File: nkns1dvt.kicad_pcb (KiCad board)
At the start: 2 copper layers, 180.4 x 132.8 mm, 76 parts, among them J1 MJ-4PP-9, J2 SERIAL_LED, SW1 SW_RESET, SW10 SW_PUSH, SW11 SW_PUSH, SW12 SW_PUSH, SW13 SW_PUSH, SW14 SW_PUSH, SW15 SW_PUSH, SW16 SW_PUSH, SW17 SW_PUSH, SW18 SW_PUSH, SW19 SW_PUSH, SW2 SW_PUSH, SW20 SW_PUSH, SW21 SW_PUSH, SW22 SW_PUSH, SW23 SW_PUSH, SW24 SW_PUSH, SW25 SW_PUSH, SW26 SW_PUSH, SW27 SW_PUSH, SW28 SW_PUSH, SW29 SW_PUSH, SW3 SW_PUSH, SW30 SW_PUSH, SW31 SW_PUSH, SW32 SW_PUSH, SW33 SW_PUSH, SW34 SW_PUSH, SW4 SW_PUSH, SW5 SW_PUSH, SW6 SW_PUSH, SW7 SW_PUSH, SW8 SW_PUSH, SW9 SW_PUSH, U1 ProMicro

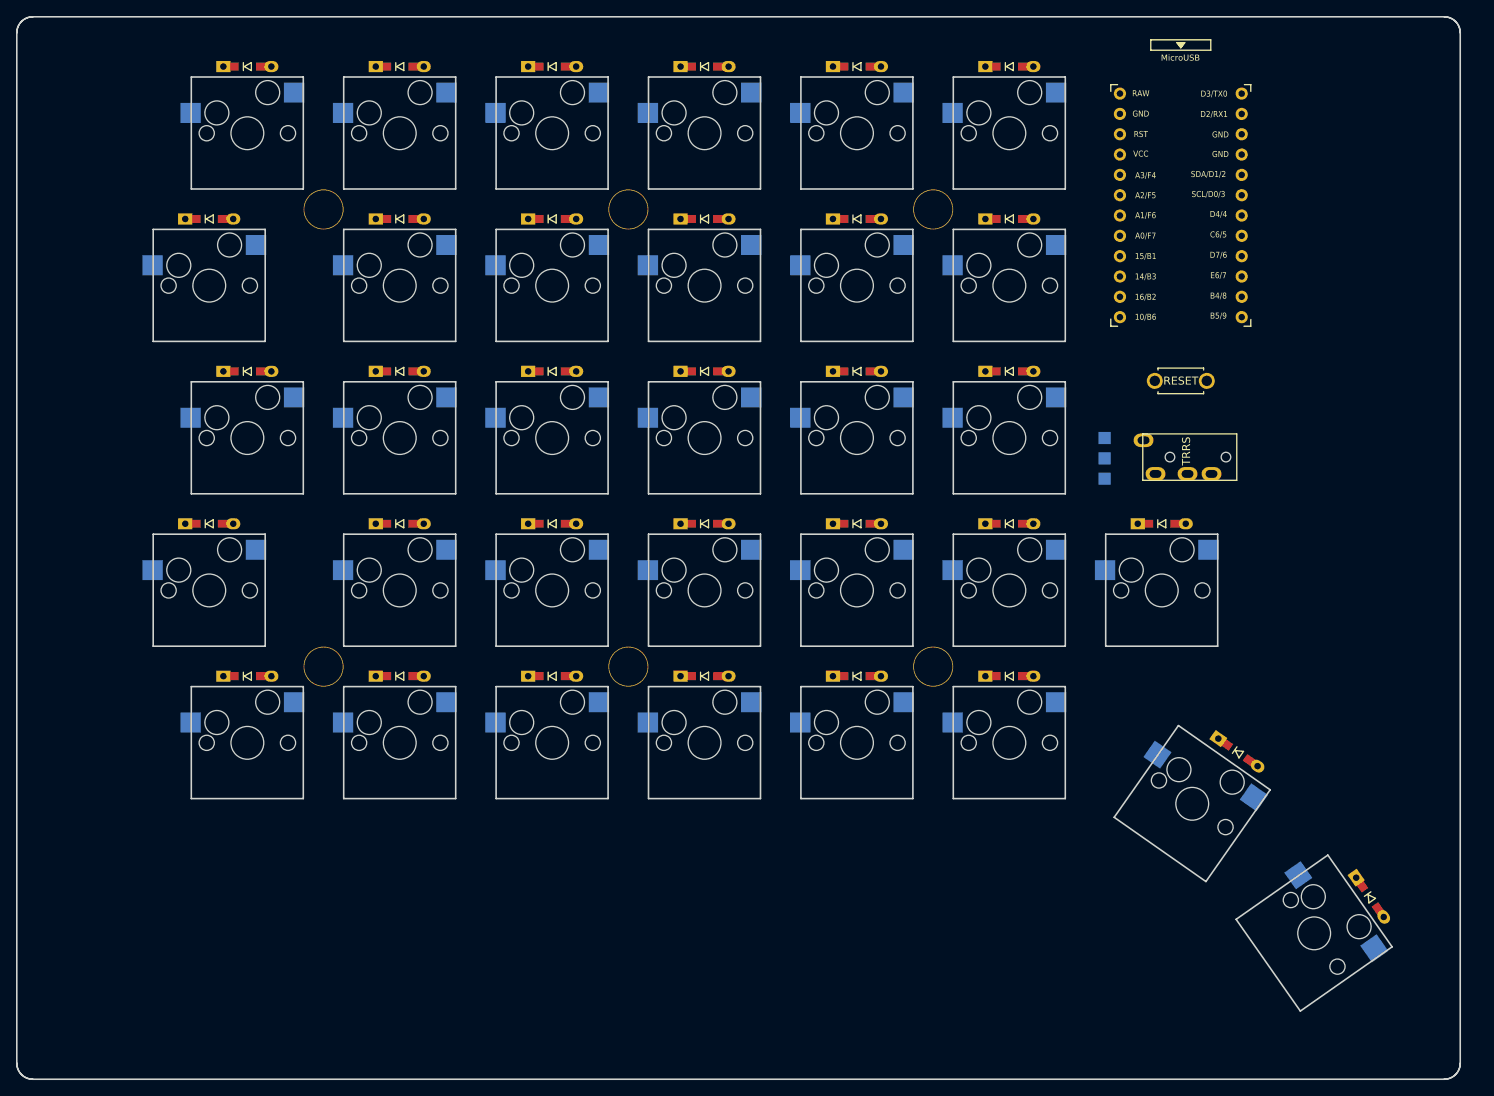
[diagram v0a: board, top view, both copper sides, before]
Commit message: Change promicro footprint Change edge layer
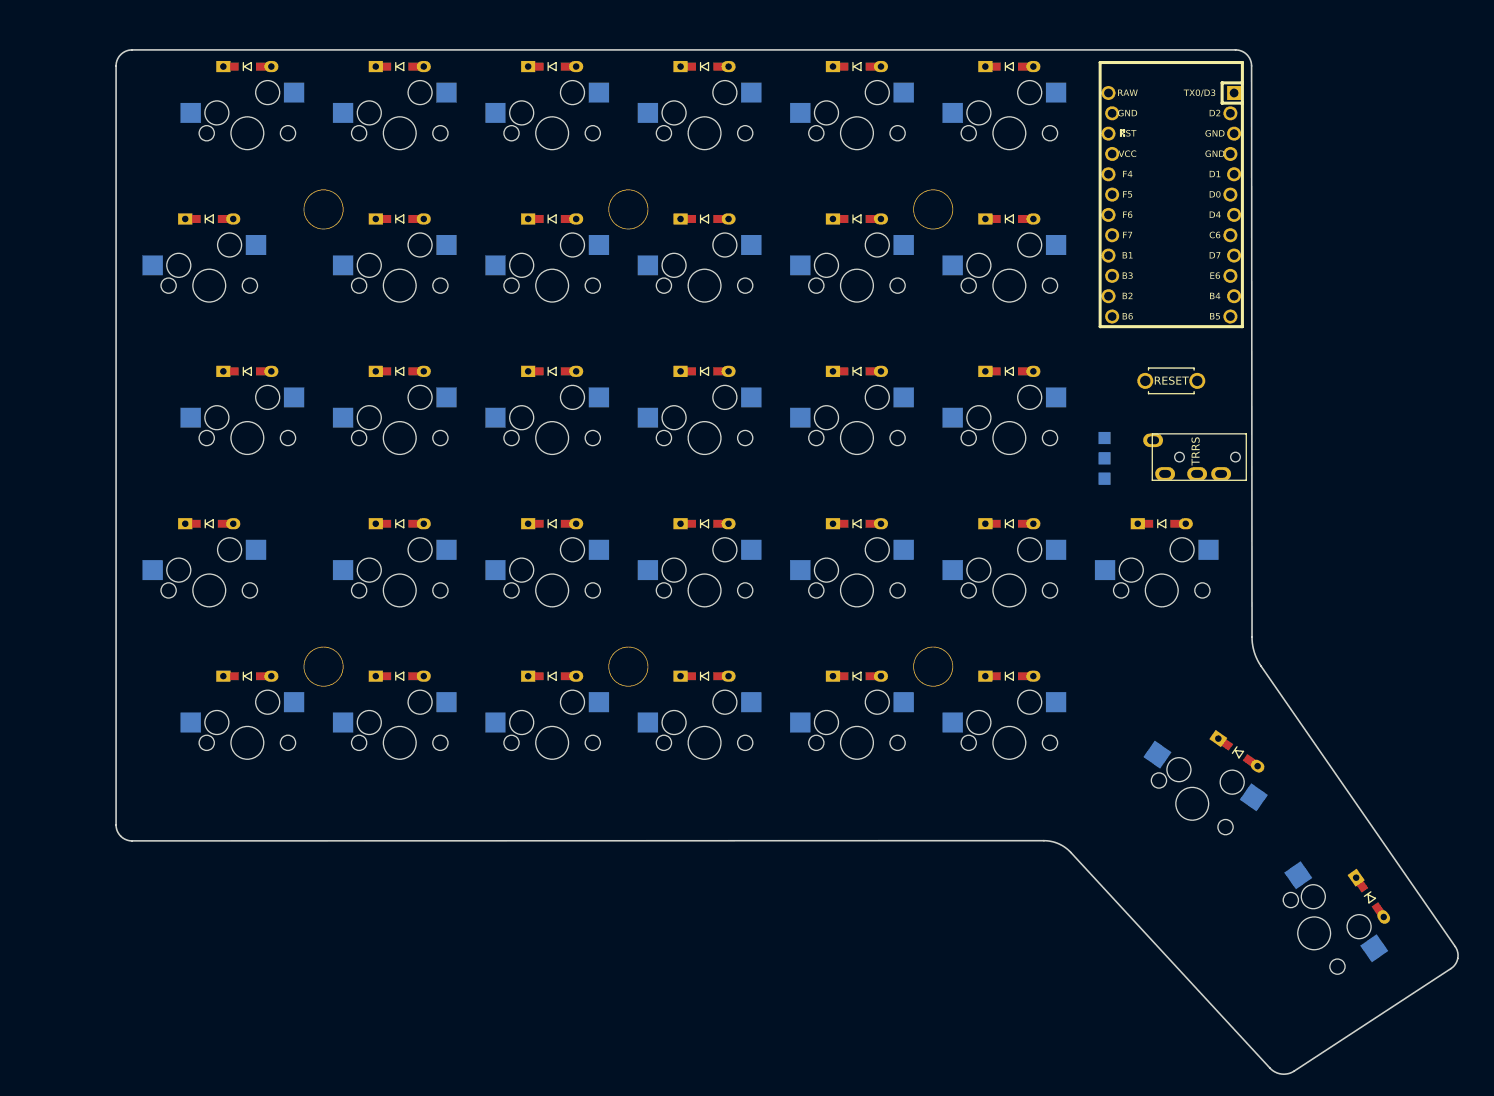
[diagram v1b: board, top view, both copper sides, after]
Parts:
- U1: footprint kbd:ProMicro_v3 -> Keebio-Parts:ArduinoProMicro-ZigZag; moved to B.Cu
- moved U1 1.33 mm to (161.7, 40.6), turned to 270 degrees
- moved J1 1.19 mm to (171.3, 72.2)
- moved SW1 1.19 mm to (161.7, 62.7)
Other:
- board size 180.4 x 132.8 mm -> 167.7 x 128 mm

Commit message: Modify LED. Add GND/VCC route.
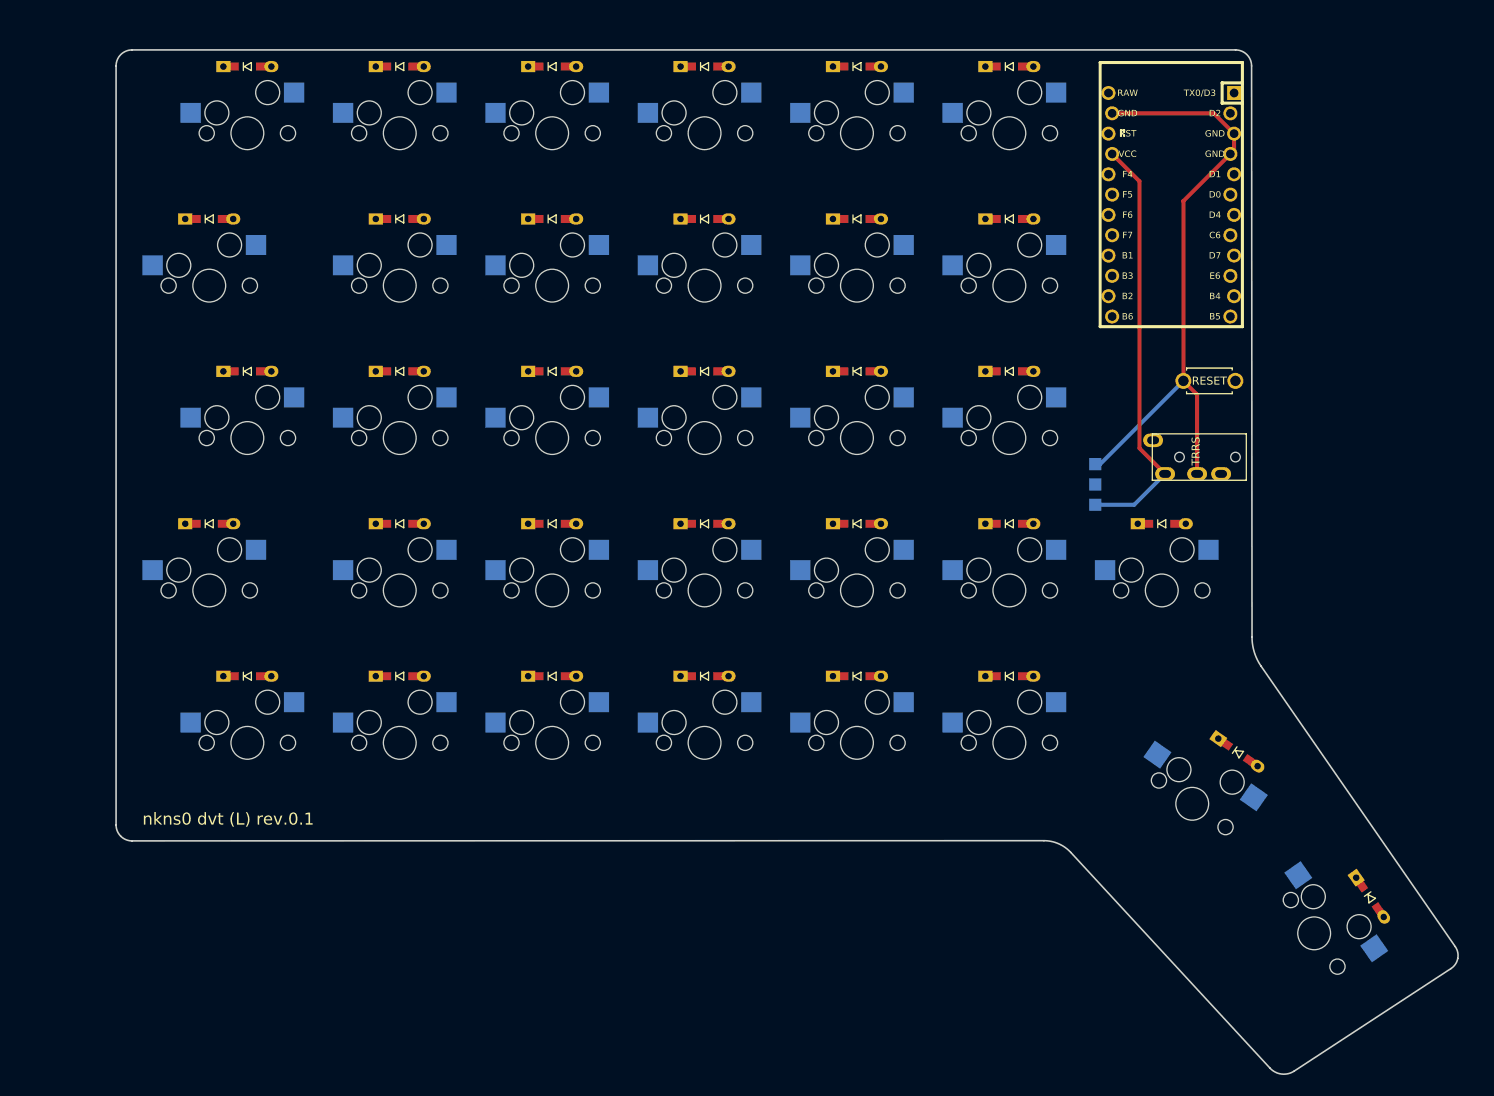
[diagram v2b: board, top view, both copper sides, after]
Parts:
- removed Ref** (x6): Val**, kbd:HOLE
- moved SW1 4.76 mm to (166.5, 62.7)
- moved J2 3.46 mm to (152.2, 78.1)
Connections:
- J1 pad A: Net-(J1-PadA) -> (no net)
- J2 pad 1: GND -> VCC
- J2 pad 3: VCC -> GND
- U1 pad 13: Net-(U1-Pad13) -> (no net)
- U1 pad 19: Net-(U1-Pad19) -> (no net)
- U1 pad 20: Net-(U1-Pad20) -> (no net)
- U1 pad 24: Net-(U1-Pad24) -> (no net)
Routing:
- net GND: track 0.00 -> 77.8 mm
- net VCC: track 0.00 -> 53.1 mm
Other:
- board text added: "nkns0 dvt (L) rev.0.1"

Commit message: Change to reversible.
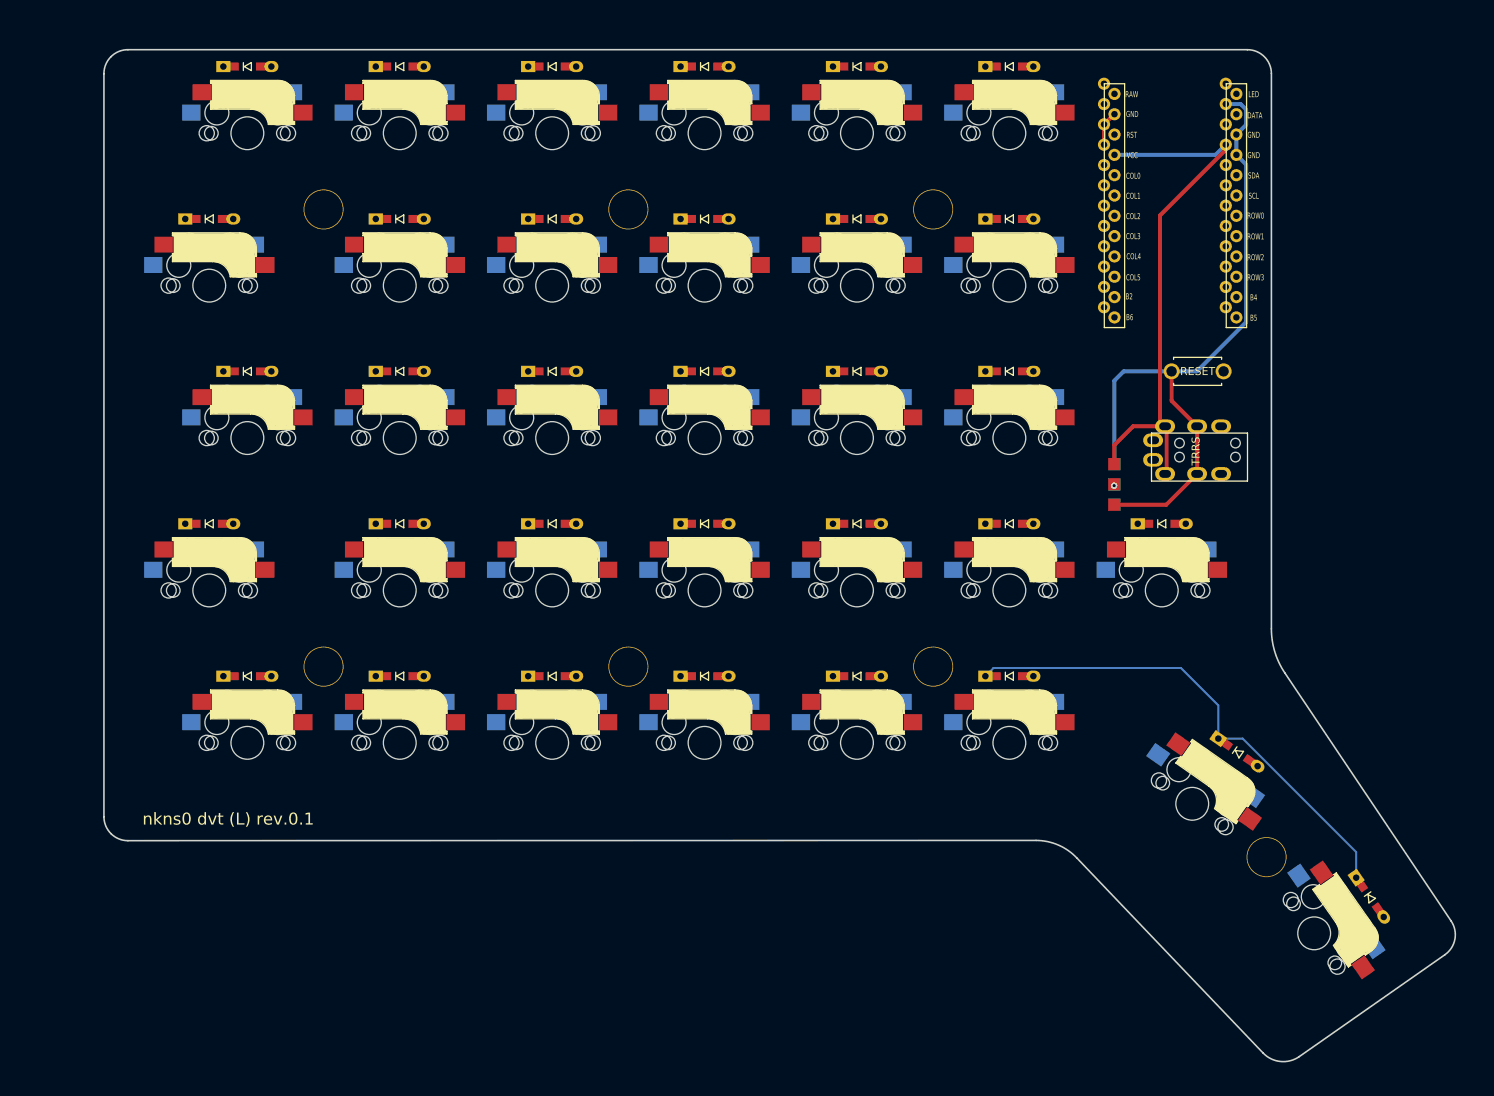
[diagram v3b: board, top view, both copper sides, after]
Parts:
- added Hole1: , kbd:HOLE, F.Cu at (55.8, 41.2)
- added Hole2: , kbd:HOLE, F.Cu at (93.9, 41.2)
- added Hole3: , kbd:HOLE, F.Cu at (132.0, 41.2)
- added Hole4: , kbd:HOLE, F.Cu at (55.8, 98.4)
- added Hole5: , kbd:HOLE, F.Cu at (93.9, 98.4)
- added Hole6: , kbd:HOLE, F.Cu at (132.0, 98.4)
- added Hole7: , kbd:HOLE, F.Cu at (173.6, 122.2)
- J1: footprint kbd:MJ-4PP-9_1side -> kbd:MJ-4PP-9
- J2: footprint kbd:StripLED_1side -> kbd:StripLED_rev
- SW1: footprint kbd:ResetSW_1side -> kbd:ResetSW
- SW10, SW11, SW12, SW13, SW14, SW15, SW16, SW17, SW18, SW19, SW2, SW20, SW21, SW22, SW23, SW24, SW25, SW26, SW27, SW28, SW29, SW3, SW30, SW31, SW32, SW33, SW34, SW4, SW5, SW6, SW7, SW8, SW9: footprint kbd:CherryMX_Hotswap -> kbd:CherryMX_MidHeight_Hotswap
- U1: footprint Keebio-Parts:ArduinoProMicro-ZigZag -> kbd:ProMicro_v2
- moved J2 2.38 mm to (154.6, 78.1)
- moved SW1 1.89 mm to (165.0, 61.5)
- moved U1 0.99 mm to (161.0, 40.0), turned to 180 degrees
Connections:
- J1 pad A: (no net) -> Net-(J1-PadA)
- U1 pad 13: (no net) -> Net-(U1-Pad13)
- U1 pad 19: (no net) -> Net-(U1-Pad19)
- U1 pad 20: (no net) -> Net-(U1-Pad20)
- U1 pad 24: (no net) -> Net-(U1-Pad24)
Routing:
- net row4: track 0.00 -> 61.9 mm
- net VCC: track 53.1 -> 69.5 mm
- net GND: track 77.8 -> 90.8 mm
- net led: track 0.00 -> 0.03 mm, vias 0 -> 1
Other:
- board size 167.7 x 128 mm -> 168.9 x 126.5 mm

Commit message: Handwired
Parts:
- moved J2 37.5 mm to (152.2, 115.6)
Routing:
- net col0: track 0.00 -> 180.0 mm, vias 0 -> 5
- net col3: track 0.00 -> 168.5 mm, vias 0 -> 5
- net col4: track 0.00 -> 168.2 mm, vias 0 -> 5
- net col5: track 0.00 -> 168.0 mm, vias 0 -> 5
- net col2: track 0.00 -> 167.9 mm, vias 0 -> 5
- net col1: track 0.00 -> 167.9 mm, vias 0 -> 5
- net row3: track 0.00 -> 124.1 mm
- net row1: track 0.00 -> 108.3 mm
- net row4: track 61.9 -> 165.7 mm
- net row0: track 0.00 -> 99.5 mm
- net row2: track 0.00 -> 99.5 mm
- net VCC: track 69.5 -> 125.8 mm, vias 0 -> 1
- net col6: track 0.00 -> 45.2 mm, vias 0 -> 2
- net GND: track 90.8 -> 116.2 mm, vias 0 -> 1
- net col7: track 0.00 -> 21.6 mm, vias 0 -> 1
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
